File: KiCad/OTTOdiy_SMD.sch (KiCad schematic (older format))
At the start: 27 parts, among them J201 Raspberry Pi Connector

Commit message: Fixes for external battery board and Routing started
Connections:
- net labels added: +5V_RASPI, GPIO16_RASPI, GPIO17_RASPI, GPIO26_RASPI, GPIO27_RASPI, PWM1_GPIO13_RASPI
- net labels removed: +5V_PI, RPI_PWM1_GPIO13
- wire segments 73 -> 75
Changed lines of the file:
@@
 +3V3_RASPI
 Text GLabel 7700 4000 0    50   Input ~ 0
-+5V_PI
++5V_RASPI
 $Comp
 L power:GND #PWR0202
@@
 I2C_SCL
 Wire Wire Line
-	7700 6000 7800 6000
-Wire Wire Line
-	7700 6100 7800 6100
-Wire Wire Line
 	7700 5600 7800 5600
 Wire Wire Line
@@
 Text GLabel 7700 5600 0    50   BiDi ~ 0
 TRIGGER1
-Text GLabel 7700 6000 0    50   BiDi ~ 0
+Text GLabel 7700 5700 0    50   BiDi ~ 0
 TRIGGER2
-Text GLabel 7700 6100 0    50   BiDi ~ 0
+Text GLabel 7700 5800 0    50   BiDi ~ 0
 TRIGGER3
 Wire Wire Line
@@
 $EndComp
 Text Label 9550 6250 0    50   ~ 0
-RPI_PWM1_GPIO13
+PWM1_GPIO13_RASPI
 Wire Wire Line
 	9400 6200 9450 6200
@@
 L Connector:TestPoint TP4
 U 1 1 5EB31494
-P 7150 4750
-F 0 "TP4" V 7250 5000 50  0000 C CNN
-F 1 "TestPoint" V 7150 5100 50  0000 C CNN
-F 2 "TestPoint:TestPoint_Keystone_5000-5004_Miniature" H 7350 4750 50  0001 C CNN
-F 3 "N/A" H 7350 4750 50  0001 C CNN
-F 4 "DNP" H 7150 4750 50  0001 C CNN "AssemblyOption"
-F 5 "N/A" H 7150 4750 50  0001 C CNN "MPN"
-F 6 "N/A" H 7150 4750 50  0001 C CNN "Manufacturer"
-F 7 "$0.00" H 7150 4750 50  0001 C CNN "UnitCost(USD)"
-	1    7150 4750
+P 6500 4750
+F 0 "TP4" V 6600 5000 50  0000 C CNN
+F 1 "TestPoint" V 6500 5100 50  0000 C CNN
+F 2 "TestPoint:TestPoint_Keystone_5000-5004_Miniature" H 6700 4750 50  0001 C CNN
+F 3 "N/A" H 6700 4750 50  0001 C CNN
+F 4 "DNP" H 6500 4750 50  0001 C CNN "AssemblyOption"
+F 5 "N/A" H 6500 4750 50  0001 C CNN "MPN"
+F 6 "N/A" H 6500 4750 50  0001 C CNN "Manufacturer"
+F 7 "$0.00" H 6500 4750 50  0001 C CNN "UnitCost(USD)"
+	1    6500 4750
 	0    -1   -1   0
 $EndComp
@@
 L Connector:TestPoint TP5
 U 1 1 5EB322D2
-P 7150 4900
-F 0 "TP5" V 7196 5087 50  0000 L CNN
-F 1 "TestPoint" V 7105 5087 50  0000 L CNN
-F 2 "TestPoint:TestPoint_Keystone_5000-5004_Miniature" H 7350 4900 50  0001 C CNN
-F 3 "N/A" H 7350 4900 50  0001 C CNN
-F 4 "DNP" H 7150 4900 50  0001 C CNN "AssemblyOption"
-F 5 "N/A" H 7150 4900 50  0001 C CNN "MPN"
-F 6 "N/A" H 7150 4900 50  0001 C CNN "Manufacturer"
-F 7 "$0.00" H 7150 4900 50  0001 C CNN "UnitCost(USD)"
-	1    7150 4900
+P 6500 4900
+F 0 "TP5" V 6546 5087 50  0000 L CNN
+F 1 "TestPoint" V 6455 5087 50  0000 L CNN
+F 2 "TestPoint:TestPoint_Keystone_5000-5004_Miniature" H 6700 4900 50  0001 C CNN
+F 3 "N/A" H 6700 4900 50  0001 C CNN
+F 4 "DNP" H 6500 4900 50  0001 C CNN "AssemblyOption"
+F 5 "N/A" H 6500 4900 50  0001 C CNN "MPN"
+F 6 "N/A" H 6500 4900 50  0001 C CNN "Manufacturer"
+F 7 "$0.00" H 6500 4900 50  0001 C CNN "UnitCost(USD)"
+	1    6500 4900
 	0    -1   -1   0
 $EndComp
 Wire Wire Line
-	7150 4900 7800 4900
+	6500 4900 7800 4900
 Wire Wire Line
 	7800 4800 7350 4800
@@
 	7350 4800 7350 4750
 Wire Wire Line
-	7350 4750 7150 4750
+	7350 4750 6500 4750
 $Comp
 L Connector:TestPoint TP2
 U 1 1 5EB37B7C
-P 7100 5600
-F 0 "TP2" V 7146 5787 50  0000 L CNN
-F 1 "TestPoint" V 7055 5787 50  0000 L CNN
-F 2 "TestPoint:TestPoint_Keystone_5000-5004_Miniature" H 7300 5600 50  0001 C CNN
-F 3 "N/A" H 7300 5600 50  0001 C CNN
-F 4 "DNP" H 7100 5600 50  0001 C CNN "AssemblyOption"
-F 5 "N/A" H 7100 5600 50  0001 C CNN "MPN"
-F 6 "N/A" H 7100 5600 50  0001 C CNN "Manufacturer"
-F 7 "$0.00" H 7100 5600 50  0001 C CNN "UnitCost(USD)"
-	1    7100 5600
+P 6500 6400
+F 0 "TP2" V 6546 6587 50  0000 L CNN
+F 1 "TestPoint" V 6455 6587 50  0000 L CNN
+F 2 "TestPoint:TestPoint_Keystone_5000-5004_Miniature" H 6700 6400 50  0001 C CNN
+F 3 "N/A" H 6700 6400 50  0001 C CNN
+F 4 "DNP" H 6500 6400 50  0001 C CNN "AssemblyOption"
+F 5 "N/A" H 6500 6400 50  0001 C CNN "MPN"
+F 6 "N/A" H 6500 6400 50  0001 C CNN "Manufacturer"
+F 7 "$0.00" H 6500 6400 50  0001 C CNN "UnitCost(USD)"
+	1    6500 6400
 	0    -1   -1   0
 $EndComp
@@
 L Connector:TestPoint TP3
 U 1 1 5EB385D3
-P 7100 5800
-F 0 "TP3" V 7146 5987 50  0000 L CNN
-F 1 "TestPoint" V 7055 5987 50  0000 L CNN
-F 2 "TestPoint:TestPoint_Keystone_5000-5004_Miniature" H 7300 5800 50  0001 C CNN
-F 3 "N/A" H 7300 5800 50  0001 C CNN
-F 4 "DNP" H 7100 5800 50  0001 C CNN "AssemblyOption"
-F 5 "N/A" H 7100 5800 50  0001 C CNN "MPN"
-F 6 "N/A" H 7100 5800 50  0001 C CNN "Manufacturer"
-F 7 "$0.00" H 7100 5800 50  0001 C CNN "UnitCost(USD)"
-	1    7100 5800
+P 6500 6600
+F 0 "TP3" V 6546 6787 50  0000 L CNN
+F 1 "TestPoint" V 6455 6787 50  0000 L CNN
+F 2 "TestPoint:TestPoint_Keystone_5000-5004_Miniature" H 6700 6600 50  0001 C CNN
+F 3 "N/A" H 6700 6600 50  0001 C CNN
+F 4 "DNP" H 6500 6600 50  0001 C CNN "AssemblyOption"
+F 5 "N/A" H 6500 6600 50  0001 C CNN "MPN"
+F 6 "N/A" H 6500 6600 50  0001 C CNN "Manufacturer"
+F 7 "$0.00" H 6500 6600 50  0001 C CNN "UnitCost(USD)"
+	1    6500 6600
 	0    -1   -1   0
 $EndComp
@@
 	7200 5900 7800 5900
 Wire Wire Line
-	7100 5800 7800 5800
-Wire Wire Line
-	7800 5700 7200 5700
-Wire Wire Line
-	7200 5700 7200 5600
-Wire Wire Line
-	7200 5600 7100 5600
+	7700 5800 7800 5800
+Wire Wire Line
+	7800 5700 7700 5700
 $Bitmap
 Pos 15400 10300
@@
 EndData
 $EndBitmap
+Text Label 7150 4750 2    50   ~ 0
+GPIO16_RASPI
+Text Label 7150 4900 2    50   ~ 0
+GPIO17_RASPI
+Wire Wire Line
+	7300 6000 7300 6400
+Wire Wire Line
+	7300 6400 6500 6400
+Wire Wire Line
+	7300 6000 7800 6000
+Wire Wire Line
+	7400 6100 7400 6600
+Wire Wire Line
+	7400 6600 6500 6600
+Wire Wire Line
+	7400 6100 7800 6100
+Text Label 7150 6400 2    50   ~ 0
+GPIO26_RASPI
+Text Label 7150 6600 2    50   ~ 0
+GPIO27_RASPI
 $EndSCHEMATC

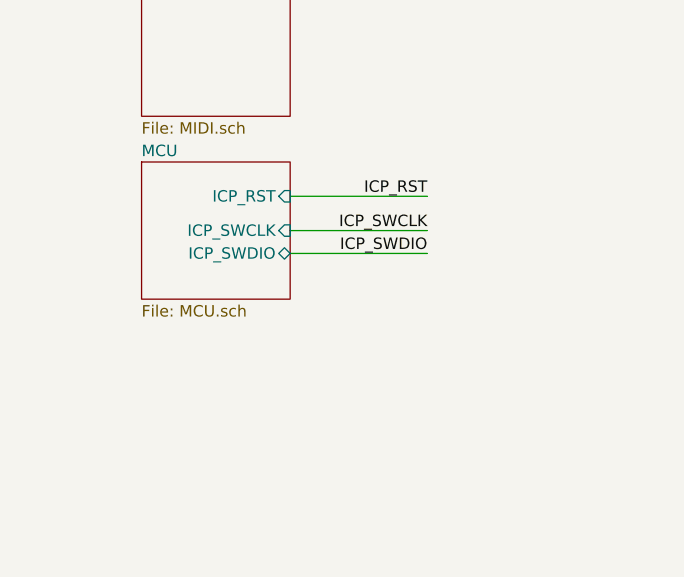
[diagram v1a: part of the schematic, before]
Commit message: Add SP3T style DP3T footprint and some schematic labels
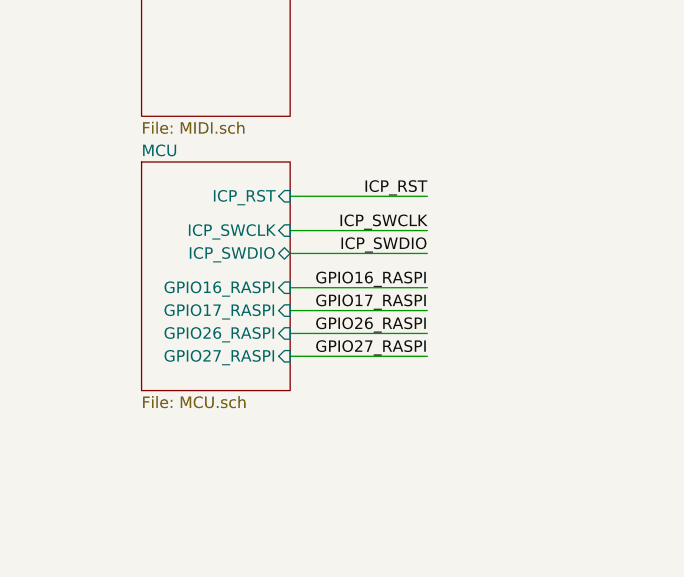
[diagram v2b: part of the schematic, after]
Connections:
- wire segments 75 -> 79
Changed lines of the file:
@@
 Comment4 ""
 $EndDescr
-$Sheet
-S 2450 3900 650  600
-U 5C4320DF
-F0 "MCU" 50
-F1 "MCU.sch" 50
-F2 "ICP_SWCLK" I R 3100 4200 50
-F3 "ICP_SWDIO" B R 3100 4300 50
-F4 "ICP_RST" I R 3100 4050 50
-$EndSheet
 Text GLabel 9550 4000 2    50   Output ~ 0
 +3V3_RASPI
@@
 Text Label 7150 6600 2    50   ~ 0
 GPIO27_RASPI
+Wire Wire Line
+	3100 4450 3700 4450
+Wire Wire Line
+	3100 4550 3700 4550
+Wire Wire Line
+	3100 4650 3700 4650
+Wire Wire Line
+	3100 4750 3700 4750
+Text Label 3700 4450 2    50   ~ 0
+GPIO16_RASPI
+Text Label 3700 4550 2    50   ~ 0
+GPIO17_RASPI
+Text Label 3700 4650 2    50   ~ 0
+GPIO26_RASPI
+Text Label 3700 4750 2    50   ~ 0
+GPIO27_RASPI
+$Sheet
+S 2450 3900 650  1000
+U 5C4320DF
+F0 "MCU" 50
+F1 "MCU.sch" 50
+F2 "ICP_SWCLK" I R 3100 4200 50
+F3 "ICP_SWDIO" B R 3100 4300 50
+F4 "ICP_RST" I R 3100 4050 50
+F5 "GPIO26_RASPI" I R 3100 4650 50
+F6 "GPIO27_RASPI" I R 3100 4750 50
+F7 "GPIO17_RASPI" I R 3100 4550 50
+F8 "GPIO16_RASPI" I R 3100 4450 50
+$EndSheet
 $EndSCHEMATC

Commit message: routed buck boost supply
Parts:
- removed TP2, TP3, TP4, TP5: TestPoint, TestPoint:TestPoint_Keystone_5000-5004_Miniature, symbol Connector:TestPoint
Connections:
- net labels added: AMP_ENABLE, GPIO0_RASPI, GPIO1_RASPI, HP_SENSE, LI_SENSE, LO_SENSE
- net labels removed: GPIO16_RASPI, GPIO17_RASPI, GPIO26_RASPI, GPIO27_RASPI
- wire segments 79 -> 68

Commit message: Placement of all components
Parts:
- added TP2: TestPoint, TestPoint:TestPoint_Keystone_5000-5004_Miniature, symbol Connector:TestPoint
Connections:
- net labels added: CE1_GPIO7_RASPI
- wire segments 68 -> 71
- no-connect marks 1 -> 0
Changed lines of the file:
@@
 	9400 5600 9500 5600
 Wire Wire Line
-	9400 5800 9550 5800
-Wire Wire Line
-	9400 5900 9550 5900
-Wire Wire Line
-	9550 4800 9400 4800
-Wire Wire Line
-	9550 4900 9400 4900
+	9400 5800 9600 5800
+Wire Wire Line
+	9400 5900 9600 5900
+Wire Wire Line
+	9600 4800 9400 4800
+Wire Wire Line
+	9600 4900 9400 4900
 Wire Wire Line
 	7700 4500 7800 4500
@@
 	1    0    0    -1
 $EndComp
-Text GLabel 9550 5500 2    50   Output ~ 0
+Text GLabel 9600 5550 2    50   Output ~ 0
 SPI_CS_RASPI_DISPLAY
-Text GLabel 9550 5800 2    50   Output ~ 0
+Text GLabel 9600 5800 2    50   Output ~ 0
 SPI_MOSI_RASPI
-Text GLabel 9550 5900 2    50   Output ~ 0
+Text GLabel 9600 5900 2    50   Output ~ 0
 SPI_SCLK_RASPI
 Text GLabel 7700 5000 0    50   Output ~ 0
@@
 Text GLabel 7700 5400 0    50   Output ~ 0
 I2S_DOUT
-Text GLabel 9550 4800 2    50   BiDi ~ 0
+Text GLabel 9600 4800 2    50   BiDi ~ 0
 I2C_SDA
-Text GLabel 9550 4900 2    50   BiDi ~ 0
+Text GLabel 9600 4900 2    50   BiDi ~ 0
 I2C_SCL
 Wire Wire Line
@@
 Text Notes 7950 6350 0    50   ~ 0
 Harwin M20-7912045 connector
-NoConn ~ 9400 5500
 $Comp
 L Device:R R3
@@
 Wire Wire Line
 	7700 4000 8400 4000
-Text GLabel 9550 5300 2    50   Output ~ 0
+Text GLabel 9600 5300 2    50   Output ~ 0
 PI_PWR_EN
 Text Notes 7900 7800 0    50   ~ 0
@@
 Text Notes 7900 8000 0    50   ~ 0
 GPIO0-8 are pulled up during boot time.\nGPIO9-27 are pulled down during boot time.
-Text GLabel 9550 6100 2    50   Output ~ 0
+Text GLabel 9600 6100 2    50   Output ~ 0
 BL_PWM
 Wire Wire Line
-	9400 6100 9550 6100
+	9400 6100 9600 6100
 $Sheet
 S 2450 3050 900  600
@@
 	10400 5200 11000 5200
 Wire Wire Line
-	9550 5300 9400 5300
+	9600 5300 9400 5300
 $Comp
 L Connector:TestPoint TP8
@@
 Wire Wire Line
 	9400 5700 10500 5700
-Text Label 10350 5700 2    50   ~ 0
+Text Label 9650 5700 0    50   ~ 0
 SPI_MISO_RASPI
 Wire Wire Line
-	9500 5600 9500 5500
-Wire Wire Line
-	9500 5500 9550 5500
+	9500 5600 9500 5550
+Wire Wire Line
+	9500 5550 9600 5550
 $Comp
 L Connector:TestPoint TP9
@@
 	0    1    1    0
 $EndComp
-Text Label 10350 6300 2    50   ~ 0
+Text Label 9650 6300 0    50   ~ 0
 PWM1_GPIO13_RASPI
 Wire Wire Line
@@
 Text GLabel 7700 4900 0    50   Input ~ 0
 AMP_ENABLE
+Wire Wire Line
+	9400 5500 9450 5500
+Wire Wire Line
+	9450 5500 9450 5450
+Wire Wire Line
+	9450 5450 10500 5450
+$Comp
+L Connector:TestPoint TP2
+U 1 1 5E3855CC
+P 10500 5450
+F 0 "TP2" V 10454 5638 50  0000 L CNN
+F 1 "TestPoint" V 10545 5638 50  0000 L CNN
+F 2 "TestPoint:TestPoint_Keystone_5000-5004_Miniature" H 10700 5450 50  0001 C CNN
+F 3 "N/A" H 10700 5450 50  0001 C CNN
+F 4 "DNP" H 10500 5450 50  0001 C CNN "AssemblyOption"
+F 5 "N/A" H 10500 5450 50  0001 C CNN "MPN"
+F 6 "N/A" H 10500 5450 50  0001 C CNN "Manufacturer"
+F 7 "$0.00" H 10500 5450 50  0001 C CNN "UnitCost(USD)"
+	1    10500 5450
+	0    1    1    0
+$EndComp
+Text Label 9650 5450 0    50   ~ 0
+CE1_GPIO7_RASPI
 $EndSCHEMATC

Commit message: add analog ground layout
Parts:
- added FID1, FID10, FID11, FID12, FID2, FID3, FID4, FID5, FID6, FID7, FID8, FID9: Fiducial, Fiducial:Fiducial_1mm_Mask2mm, symbol Mechanical:Fiducial
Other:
- note added: "Mounting Features"
- note added: "Optical Alignment\n"
- note added: "Raspberry Pi Model 3A+"

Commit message: misc raspi routing
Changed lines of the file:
@@
 Wire Wire Line
 	7150 4150 7800 4150
+Text GLabel 7700 5450 0    50   Input ~ 0
+LI_SENSE
 Text GLabel 7700 5350 0    50   Input ~ 0
-LI_SENSE
-Text GLabel 7700 5250 0    50   Input ~ 0
 HP_SENSE
 Wire Wire Line
 	7700 5250 7800 5250
-Text GLabel 7700 5450 0    50   Input ~ 0
+Text GLabel 7700 5250 0    50   Input ~ 0
 LO_SENSE
 Wire Wire Line

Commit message: swap 3.3V supply and 5v led switch. still needs reconnecting and cleanup
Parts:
- removed H206: MountingHole, OTTO_Footprints_Lib:Mounting_Hole_M2.5_Loose_Fit, symbol Mechanical:MountingHole
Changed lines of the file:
@@
-$EndComp
-$Comp
-L Mechanical:MountingHole H206
-U 1 1 5DE07FE5
-P 3000 9100
-F 0 "H206" H 3100 9146 50  0000 L CNN
-F 1 "MountingHole" H 3100 9055 50  0000 L CNN
-F 2 "OTTO_Footprints_Lib:Mounting_Hole_M2.5_Loose_Fit" H 3000 9100 50  0001 C CNN
-F 3 "N/A" H 3000 9100 50  0001 C CNN
-F 4 "DNP" H 3000 9100 50  0001 C CNN "AssemblyOption"
-F 5 "$0.00" H 3000 9100 50  0001 C CNN "UnitCost(USD)"
-F 6 "N/A" H 3000 9100 50  0001 C CNN "MPN"
-F 7 "N/A" H 3000 9100 50  0001 C CNN "Manufacturer"
-	1    3000 9100
-	1    0    0    -1
 $EndComp
 $Comp

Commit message: completed board
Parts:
- TP2, TP6, TP7, TP8, TP9: footprint TestPoint:TestPoint_Keystone_5000-5004_Miniature -> TestPoint:TestPoint_THTPad_D1.0mm_Drill0.5mm
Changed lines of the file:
@@
 F 0 "TP8" V 10454 5238 50  0000 L CNN
 F 1 "TestPoint" V 10545 5238 50  0000 L CNN
-F 2 "TestPoint:TestPoint_Keystone_5000-5004_Miniature" H 10700 5050 50  0001 C CNN
+F 2 "TestPoint:TestPoint_THTPad_D1.0mm_Drill0.5mm" H 10700 5050 50  0001 C CNN
 F 3 "N/A" H 10700 5050 50  0001 C CNN
 F 4 "DNP" H 10500 5050 50  0001 C CNN "AssemblyOption"
@@
 F 0 "TP9" V 10454 5838 50  0000 L CNN
 F 1 "TestPoint" V 10545 5838 50  0000 L CNN
-F 2 "TestPoint:TestPoint_Keystone_5000-5004_Miniature" H 10700 5650 50  0001 C CNN
+F 2 "TestPoint:TestPoint_THTPad_D1.0mm_Drill0.5mm" H 10700 5650 50  0001 C CNN
 F 3 "N/A" H 10700 5650 50  0001 C CNN
 F 4 "DNP" H 10500 5650 50  0001 C CNN "AssemblyOption"
@@
 F 0 "TP6" V 10350 4050 50  0000 L CNN
 F 1 "TestPoint" V 10350 4250 50  0000 L CNN
-F 2 "TestPoint:TestPoint_Keystone_5000-5004_Miniature" H 10550 3850 50  0001 C CNN
+F 2 "TestPoint:TestPoint_THTPad_D1.0mm_Drill0.5mm" H 10550 3850 50  0001 C CNN
 F 3 "N/A" H 10550 3850 50  0001 C CNN
 F 4 "DNP" H 10350 3850 50  0001 C CNN "AssemblyOption"
@@
 F 0 "TP7" V 10350 4150 50  0000 L CNN
 F 1 "TestPoint" V 10350 4350 50  0000 L CNN
-F 2 "TestPoint:TestPoint_Keystone_5000-5004_Miniature" H 10550 3950 50  0001 C CNN
+F 2 "TestPoint:TestPoint_THTPad_D1.0mm_Drill0.5mm" H 10550 3950 50  0001 C CNN
 F 3 "N/A" H 10550 3950 50  0001 C CNN
 F 4 "DNP" H 10350 3950 50  0001 C CNN "AssemblyOption"
@@
 F 0 "TP2" V 10454 4988 50  0000 L CNN
 F 1 "TestPoint" V 10545 4988 50  0000 L CNN
-F 2 "TestPoint:TestPoint_Keystone_5000-5004_Miniature" H 10700 4800 50  0001 C CNN
+F 2 "TestPoint:TestPoint_THTPad_D1.0mm_Drill0.5mm" H 10700 4800 50  0001 C CNN
 F 3 "N/A" H 10700 4800 50  0001 C CNN
 F 4 "DNP" H 10500 4800 50  0001 C CNN "AssemblyOption"
